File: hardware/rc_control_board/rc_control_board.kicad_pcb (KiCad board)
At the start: 4 copper layers, 50 x 50 mm, 53 parts, among them J1 PWR, J10 3V3_Con, J2 SWD Con, J3 I2C1, J4 GPS, J5 SPI1, J6 UART_DEBUG, J7 UART_NAV_BOARD, J8 MOTOR_CTRL, J9 SERVO_CTRL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

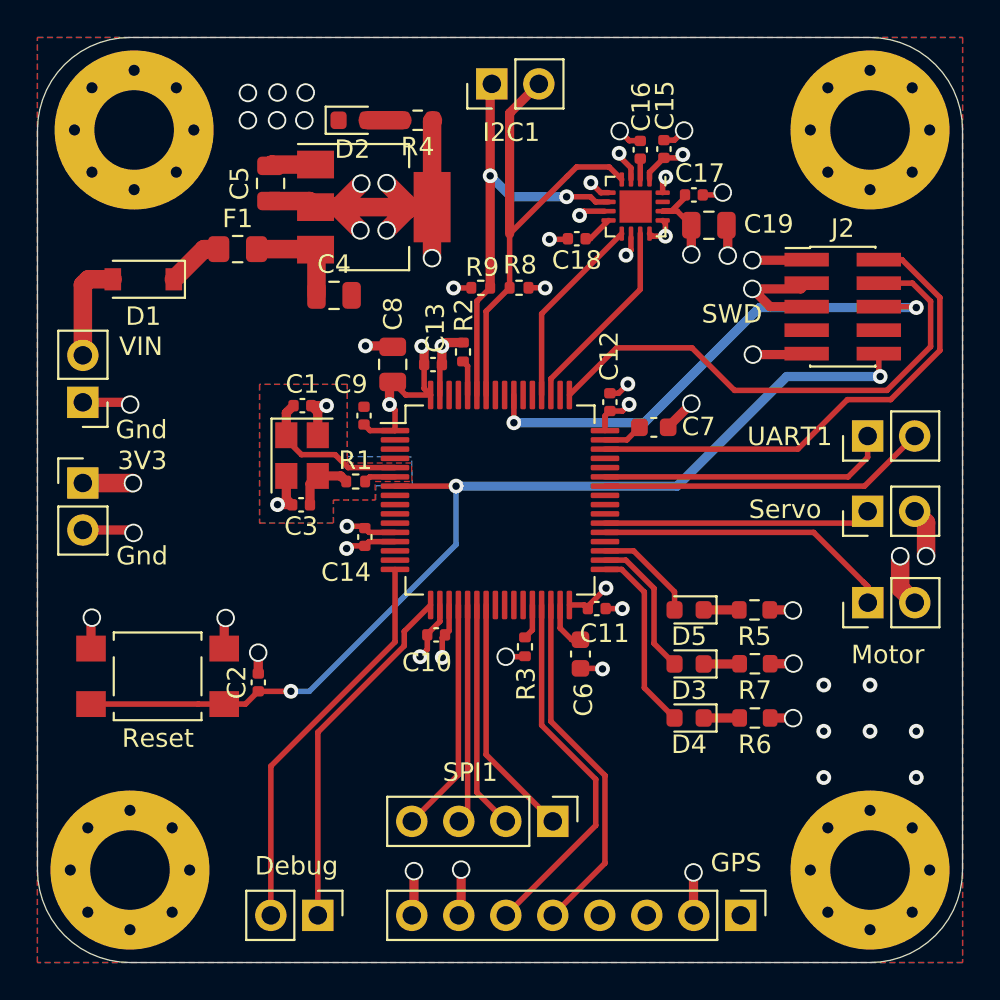
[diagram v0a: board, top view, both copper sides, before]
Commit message: HW: Fix layout errors for IMU
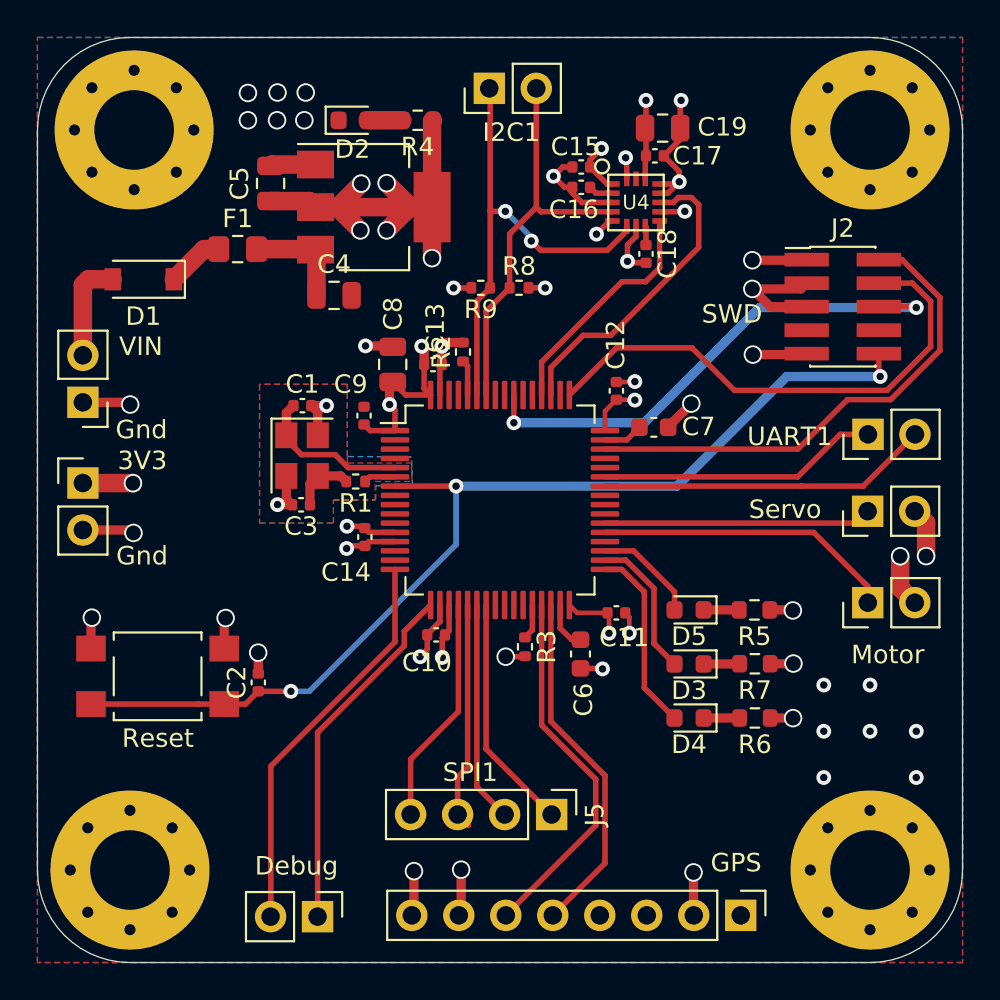
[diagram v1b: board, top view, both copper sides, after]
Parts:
- removed U3: FXOS8700CQR1, Package_DFN_QFN:QFN-16-1EP_3x3mm_P0.5mm_EP1.75x1.75mm
- added U4: FXOS8700CQ, rc_control_board:FSOS8700CQ_PKG, F.Cu at (151.0, 93.8)
- moved C19 5.81 mm to (152.4, 89.8)
- moved C15 4.57 mm to (148.1, 91.9), turned to 0 degrees
- moved C18 3.83 mm to (151.6, 96.6), turned to 270 degrees
- moved C16 3.78 mm to (148.1, 93.0), turned to 0 degrees
- moved C17 2.98 mm to (152.0, 91.3)
- moved C11 1.08 mm to (149.9, 116.0)
- moved C12 0.70 mm to (149.9, 104.0)
- moved J5 0.38 mm to (146.4, 126.9)
- moved J3 0.28 mm to (143.1, 87.7)
- moved J7 0.09 mm to (163.6, 106.4)
- moved J6 0.07 mm to (133.8, 132.4)
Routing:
- net IMU_INT1: track 9.95 -> 16.9 mm
- net GND: track 72.1 -> 77.0 mm, vias 48 -> 44
- net I2C1_SCL: track 25.8 -> 21.9 mm
- net IMU_INT2: track 10.5 -> 12.8 mm
- net I2C1_SDA: track 24.1 -> 26.1 mm
- net +3V3: track 66.2 -> 67.2 mm
- net UART1_RX: track 15.8 -> 15.2 mm
- net Net-(C18-Pad1): track 1.65 -> 1.04 mm
